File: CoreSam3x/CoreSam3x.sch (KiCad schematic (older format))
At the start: 4 parts, among them M1 PCB_GREEN_RMC, M2 LOGO_OSHW

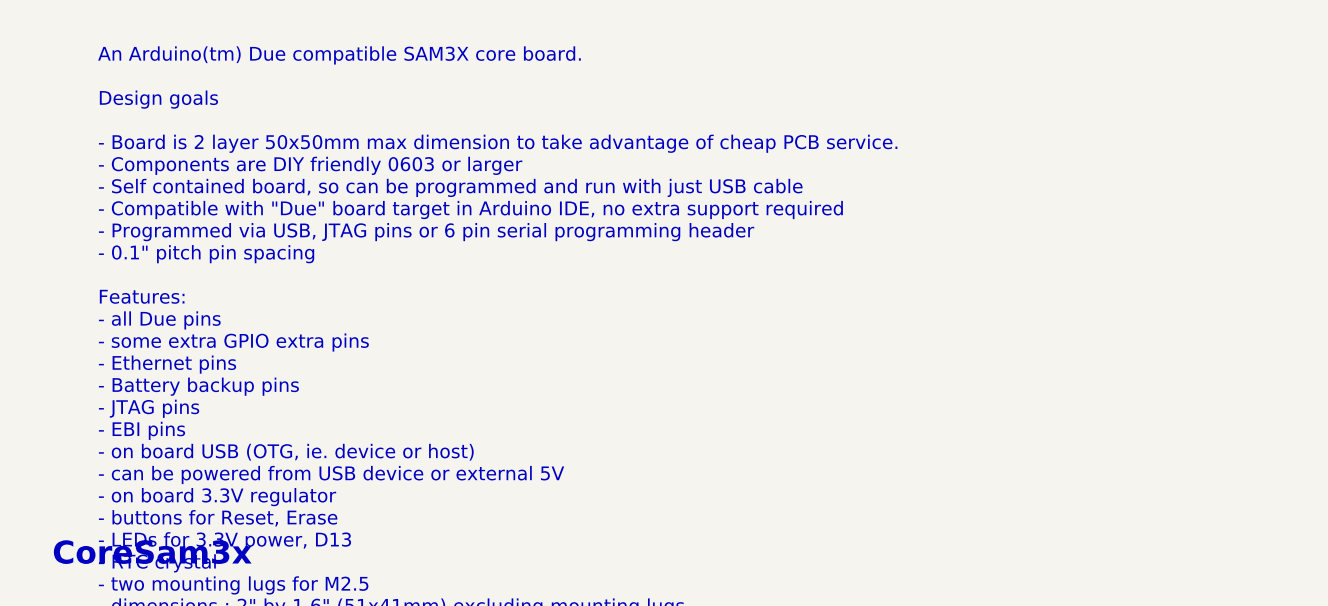
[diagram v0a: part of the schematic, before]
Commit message: CoreSam3x: improvements to layout, component selection
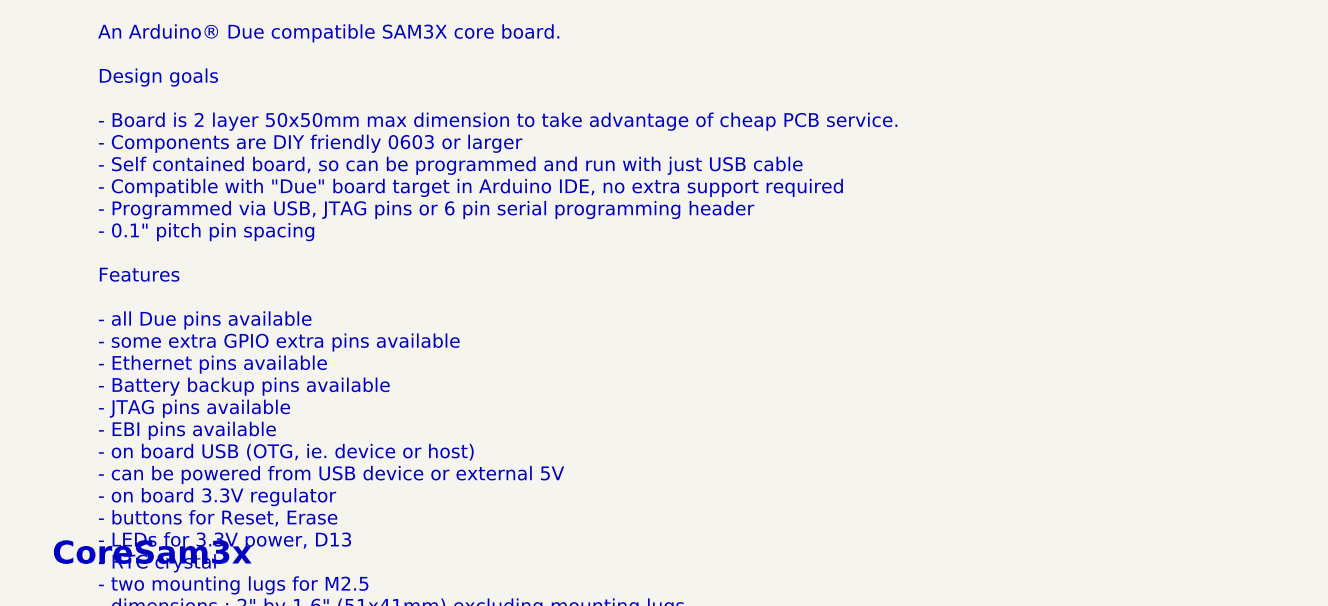
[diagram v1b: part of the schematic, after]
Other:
- note added: "An Arduino® Due compatible SAM3X core board.\n\nDesign goals\n\n- Board is 2 layer 50x50mm max dimension to take advantage of cheap PCB service.\n- Components are DIY friendly 0603 or larger\n- Self contained board, so can be programmed and run with just USB cable\n- Compatible with "Due" board target in Arduino IDE, no extra support required\n- Programmed via USB, JTAG pins or 6 pin serial progr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"
- note removed: "An Arduino(tm) Due compatible SAM3X core board.\n\nDesign goals\n\n- Board is 2 layer 50x50mm max dimension to take advantage of cheap PCB service.\n- Components are DIY friendly 0603 or larger\n- Self contained board, so can be programmed and run with just USB cable\n- Compatible with "Due" board target in Arduino IDE, no extra support required\n- Programmed via USB, JTAG pins or 6 pin serial pr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"
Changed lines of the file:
@@
 Sheet 1 3
 Title "CoreSam3x"
-Date "1 nov 2014"
+Date "2 nov 2014"
 Rev "1"
 Comp ""
@@
 CoreSam3x
 Text Notes 1950 1800 0    60   ~ 0
-An Arduino(tm) Due compatible SAM3X core board.\n\nDesign goals\n\n- Board is 2 layer 50x50mm max dimension to take advantage of cheap PCB service.\n- Components are DIY friendly 0603 or larger\n- Self contained board, so can be programmed and run with just USB cable\n- Compatible with "Due" board target in Arduino IDE, no extra support required\n- Programmed via USB, JTAG pins or 6 pin serial programming header\n- 0.1" pitch pin spacing\n\nFeatures:\n- all Due pins\n- some extra GPIO extra pins\n- Ethernet pins\n- Battery backup pins\n- JTAG pins\n- EBI pins\n- on board USB (OTG, ie. device or host)\n- can be powered from USB device or external 5V\n- on board 3.3V regulator\n- buttons for Reset, Erase\n- LEDs for 3.3V power, D13\n- RTC crystal\n- two mounting lugs for M2.5\n- dimensions : 2" by 1.6" (51x41mm) excluding mounting lugs\n\n\n"Arduino" is a trademark of Arduino LLC http://arduino.cc/
+An Arduino® Due compatible SAM3X core board.\n\nDesign goals\n\n- Board is 2 layer 50x50mm max dimension to take advantage of cheap PCB service.\n- Components are DIY friendly 0603 or larger\n- Self contained board, so can be programmed and run with just USB cable\n- Compatible with "Due" board target in Arduino IDE, no extra support required\n- Programmed via USB, JTAG pins or 6 pin serial programming header\n- 0.1" pitch pin spacing\n\nFeatures\n\n- all Due pins available\n- some extra GPIO extra pins available\n- Ethernet pins available\n- Battery backup pins available\n- JTAG pins available\n- EBI pins available\n- on board USB (OTG, ie. device or host)\n- can be powered from USB device or external 5V\n- on board 3.3V regulator\n- buttons for Reset, Erase\n- LEDs for 3.3V power, D13\n- RTC crystal\n- two mounting lugs for M2.5\n- dimensions : 2" by 1.6" (51x41mm) excluding mounting lugs\n\n\n"Arduino" is a trademark of Arduino LLC http://arduino.cc/
 $Comp
 L LOGO_OSHW M2
